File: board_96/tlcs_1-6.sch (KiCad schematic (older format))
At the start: 66 parts, among them U1 TLC5941, U2 TLC5941, U3 TLC5941

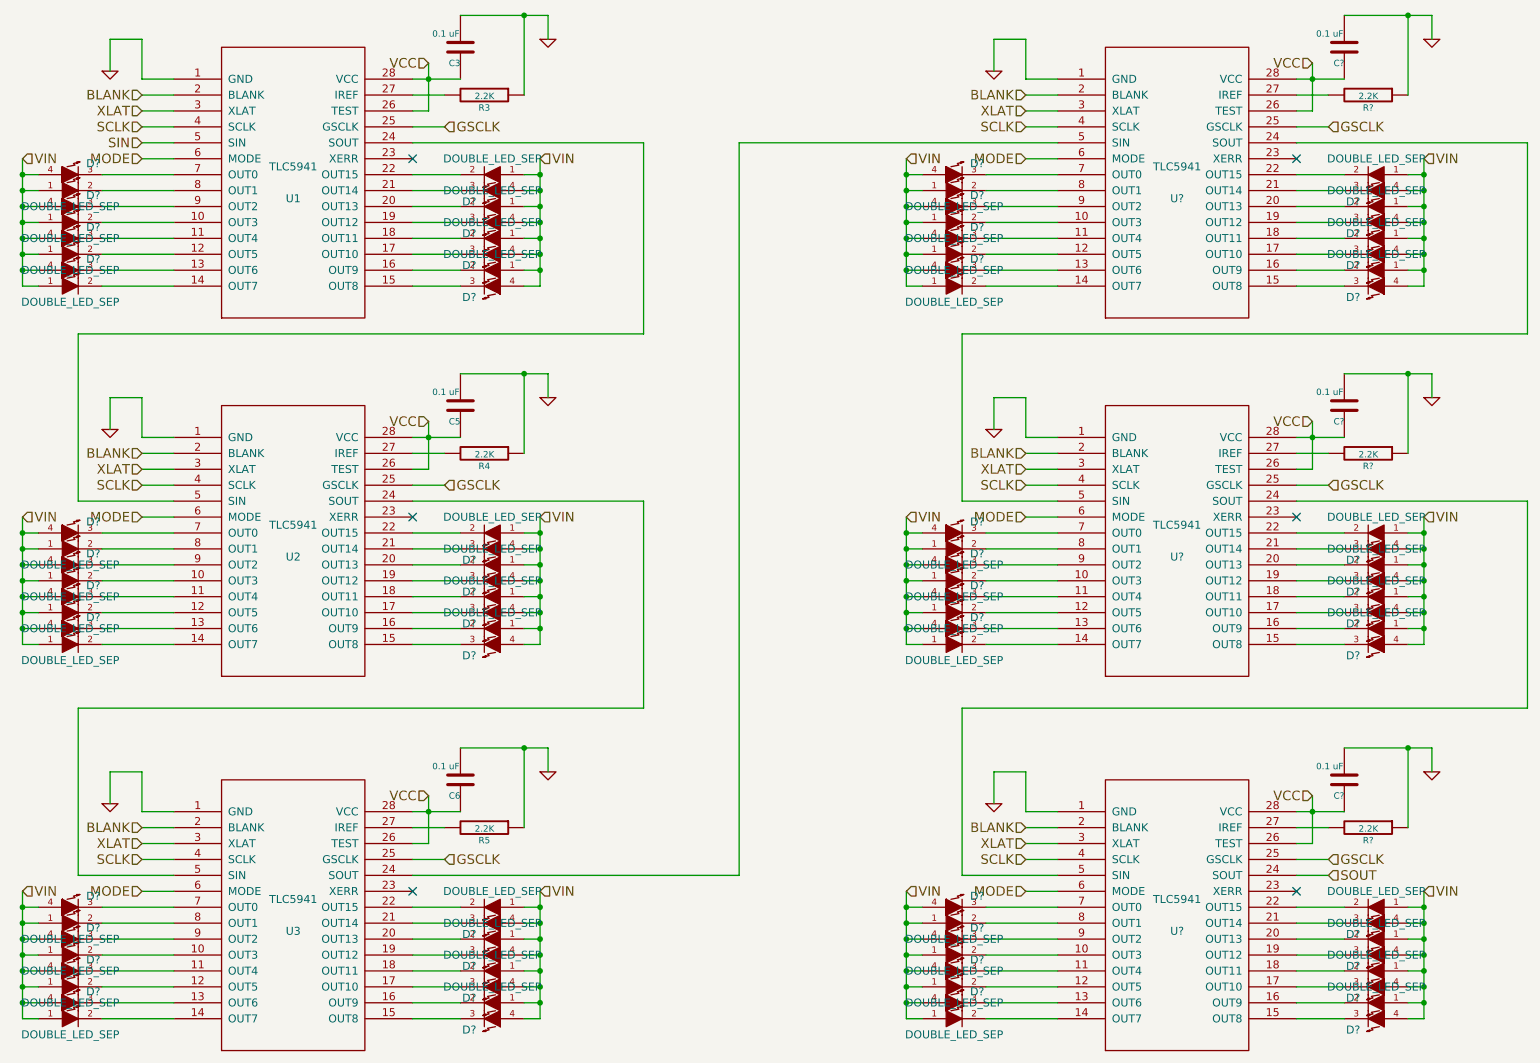
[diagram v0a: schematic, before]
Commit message: Made board_24_v2 which uses PCB-mounted LED sockets and updated various issues on board_96 as well. These PCBs were ordered around 7/1/14.
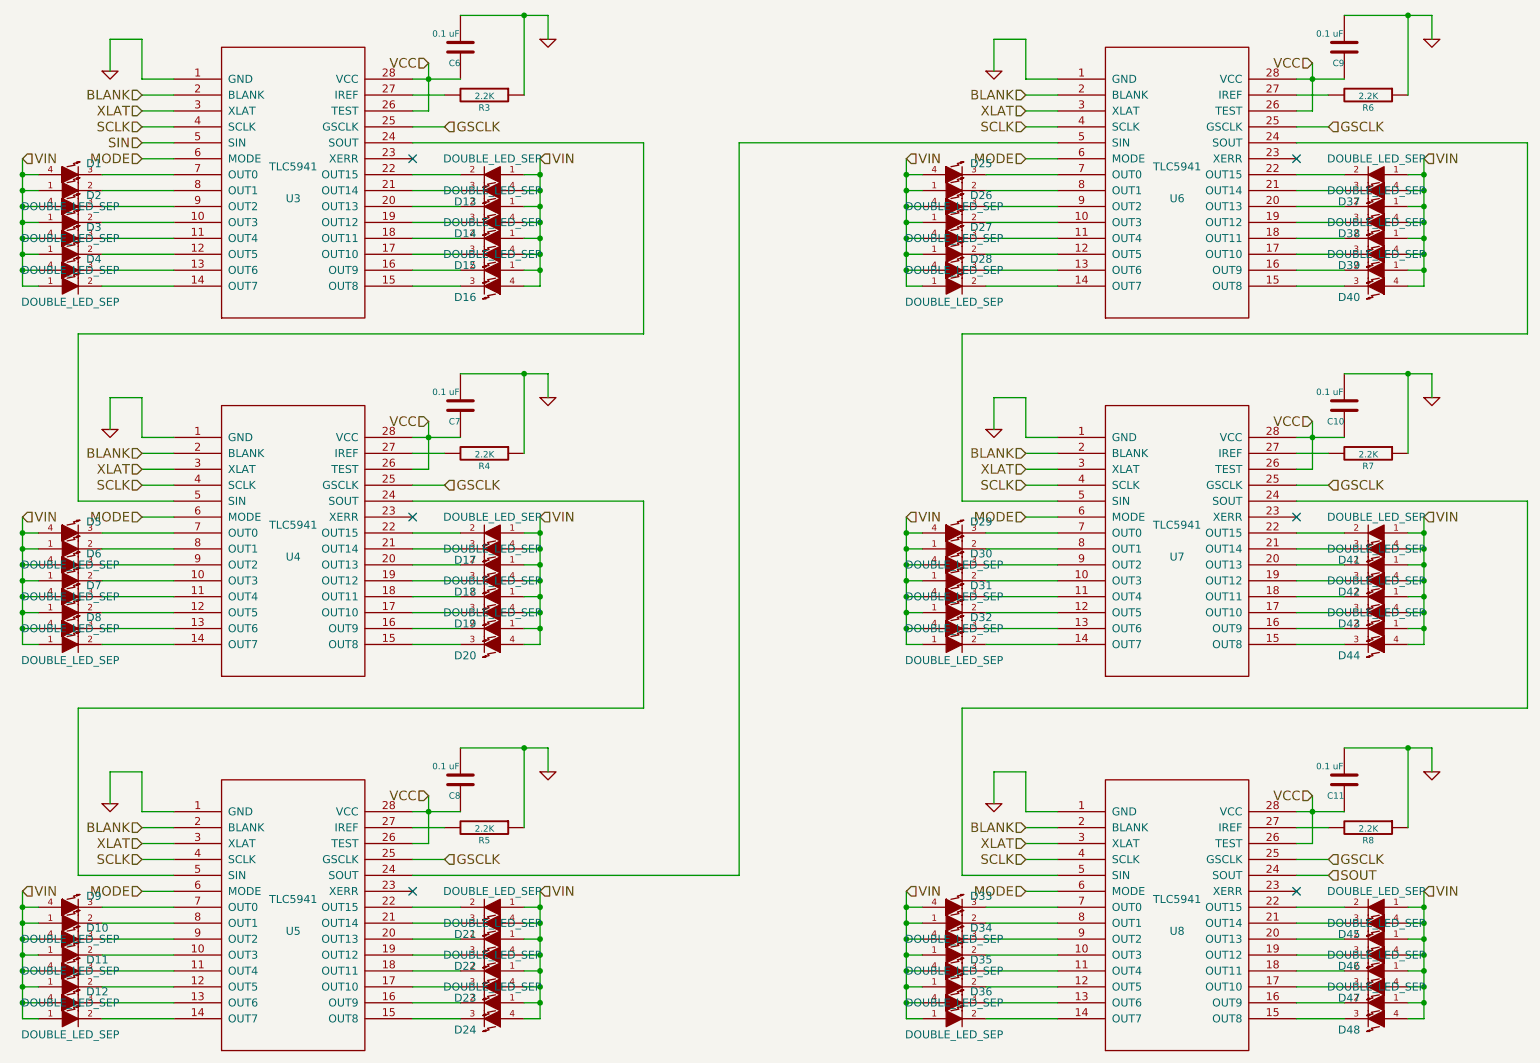
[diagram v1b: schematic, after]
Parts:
- removed C5: 0.1 uF, ~, symbol C
- removed D? (x16): DOUBLE_LED_SEP, ~, symbol DOUBLE_LED_SEP
- removed R?: 2.2K, ~, symbol R
- removed U3: TLC5941, MODULE, symbol TLC5941
- added C7: 0.1 uF, SM0805, symbol C
- added D12, D16, D17, D19, D2, D23, D3, D31, D32, D33, D34, D39, D40, D41, D42, D43: DOUBLE_LED_SEP, SMD_0805_4PIN, symbol DOUBLE_LED_SEP
- added R6: 2.2K, SM0805, symbol R
- added U5: TLC5941, TLC5940_FIXED, symbol TLC5941
- C10, C11, C9: renamed from C?; footprint ~ -> SM0805
- C6: renamed from C3; footprint ~ -> SM0805
- C8: renamed from C6; footprint ~ -> SM0805
- D1, D10, D11, D13, D14, D15, D18, D20, D21, D22, D24, D25, D26, D27, D28, D29, D30, D35, D36, D37, D38, D4, D44, D45, D46, D47, D48, D5, D6, D7, D8, D9: renamed from D?; footprint ~ -> SMD_0805_4PIN
- R3, R4, R5: footprint ~ -> SM0805
- R7, R8: renamed from R?; footprint ~ -> SM0805
- U3: renamed from U1; footprint MODULE -> TLC5940_FIXED
- U4: renamed from U2; footprint MODULE -> TLC5940_FIXED
- U6, U7, U8: renamed from U?; footprint MODULE -> TLC5940_FIXED
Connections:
- net BLANK: now also U5.2 (BLANK)
- net GND: now also C7.2, R6.1, U5.1 (GND)
- net GSCLK: now also U5.25 (GSCLK)
- net MODE: now also U5.6 (MODE)
- net SCLK: now also U5.4 (SCLK)
- net VCC: now also C7.1, U5.26 (TEST), U5.28 (VCC)
- net VIN: now also D12.1, D12.4, D16.1, D16.4, D17.1, D17.4, D19.1, D19.4, D2.1, D2.4, D23.1, D23.4, D3.1, D3.4, D31.1, D31.4, D32.1, D32.4, D33.1, D33.4, D34.1, D34.4, D39.1, D39.4, D40.1, D40.4, D41.1, D41.4, D42.1, D42.4, D43.1, D43.4
- net XLAT: now also U5.3 (XLAT)
- net at D10.2: now also U5.10 (OUT3)
- net at D11.3: now also U5.11 (OUT4)
- net at D11.2: now also U5.12 (OUT5)
- net at D24.3: now also U5.15 (OUT8)
- net at D24.2: now also U5.16 (OUT9)
- net at D22.3: now also U5.19 (OUT12)
- net at D22.2: now also U5.20 (OUT13)
- net at D21.3: now also U5.21 (OUT14)
- net at D21.2: now also U5.22 (OUT15)
- net at U6.5 (SIN): now also U5.24 (SOUT)
- net at R5.2: now also U5.27 (IREF)
- net at U4.24 (SOUT): now also U5.5 (SIN)
- net at D9.3: now also U5.7 (OUT0)
- net at D9.2: now also U5.8 (OUT1)
- net at D10.3: now also U5.9 (OUT2)
- net at U4.17 (OUT10): now also D19.3
- net at U4.18 (OUT11): now also D19.2
- net at U4.21 (OUT14): now also D17.3
- net at U4.22 (OUT15): now also D17.2
- net at U3.10 (OUT3): now also D2.2
- net at U3.11 (OUT4): now also D3.3
- net at U3.12 (OUT5): now also D3.2
- net at U3.15 (OUT8): now also D16.3
- net at U3.16 (OUT9): now also D16.2
- net at U3.9 (OUT2): now also D2.3
- net at U8.10 (OUT3): now also D34.2
- net at U8.7 (OUT0): now also D33.3
- net at U8.8 (OUT1): now also D33.2
- net at U8.9 (OUT2): now also D34.3
- net at U7.11 (OUT4): now also D31.3
- net at U7.12 (OUT5): now also D31.2
- net at U7.13 (OUT6): now also D32.3
- net at U7.14 (OUT7): now also D32.2
- net at U7.17 (OUT10): now also D43.3
- net at U7.18 (OUT11): now also D43.2
- net at U7.19 (OUT12): now also D42.3
- net at U7.20 (OUT13): now also D42.2
- net at U7.21 (OUT14): now also D41.3
- net at U7.22 (OUT15): now also D41.2
- net at U6.27 (IREF): now also R6.2
- net at U6.15 (OUT8): now also D40.3
- net at U6.16 (OUT9): now also D40.2
- net at U6.17 (OUT10): now also D39.3
- net at U6.18 (OUT11): now also D39.2
- new net: D12.3, U5.13 (OUT6)
- new net: D12.2, U5.14 (OUT7)
- new net: D23.3, U5.17 (OUT10)
- new net: D23.2, U5.18 (OUT11)
